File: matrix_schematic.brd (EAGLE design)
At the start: 84.8 x 82.5 mm, 24 parts, among them IC1 74LS595D, IC2 74LS595D, IC3 74LS595D, Q1 MOSFET-NCHANNELBS270, Q2 MOSFET-NCHANNELBS270, Q3 MOSFET-NCHANNELBS270, Q4 MOSFET-NCHANNELBS270

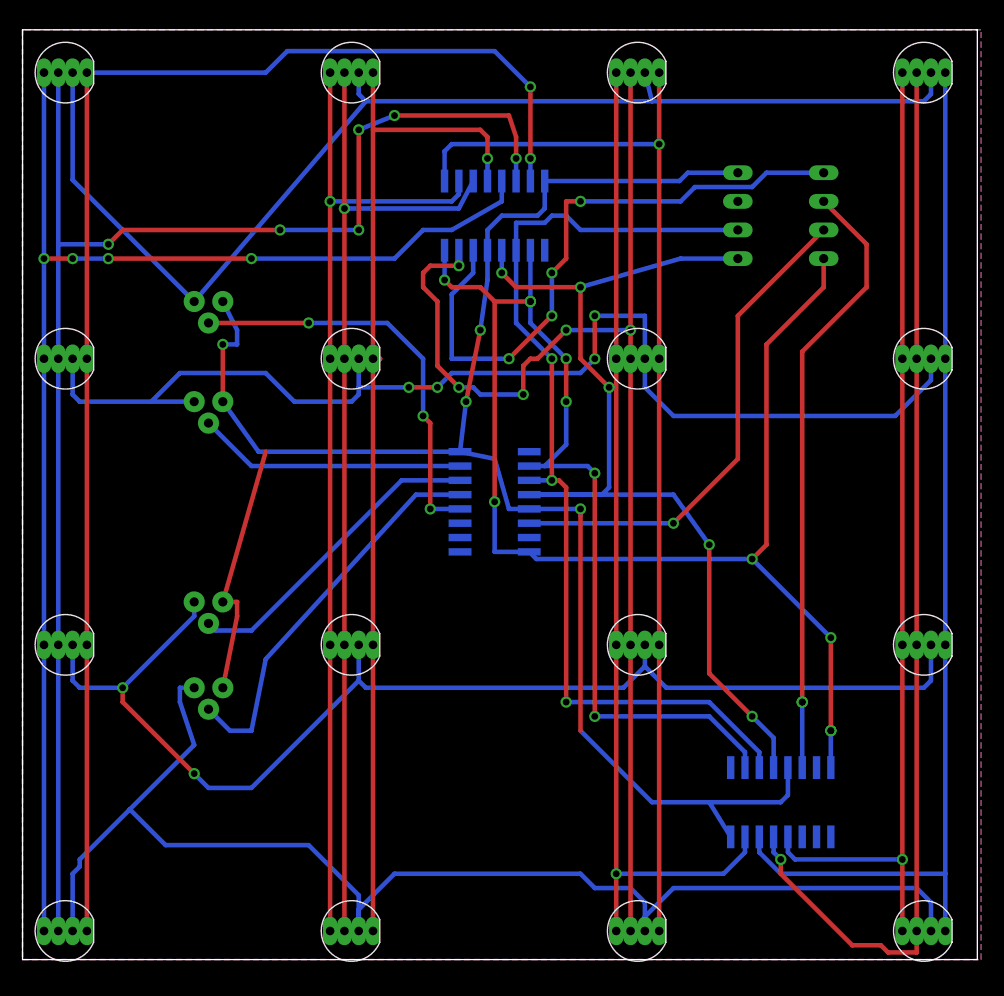
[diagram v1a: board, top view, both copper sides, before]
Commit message: Fixed a bunch of overlaps
Still many overlaps, the RGB LED footprint I used overlaps every pad.
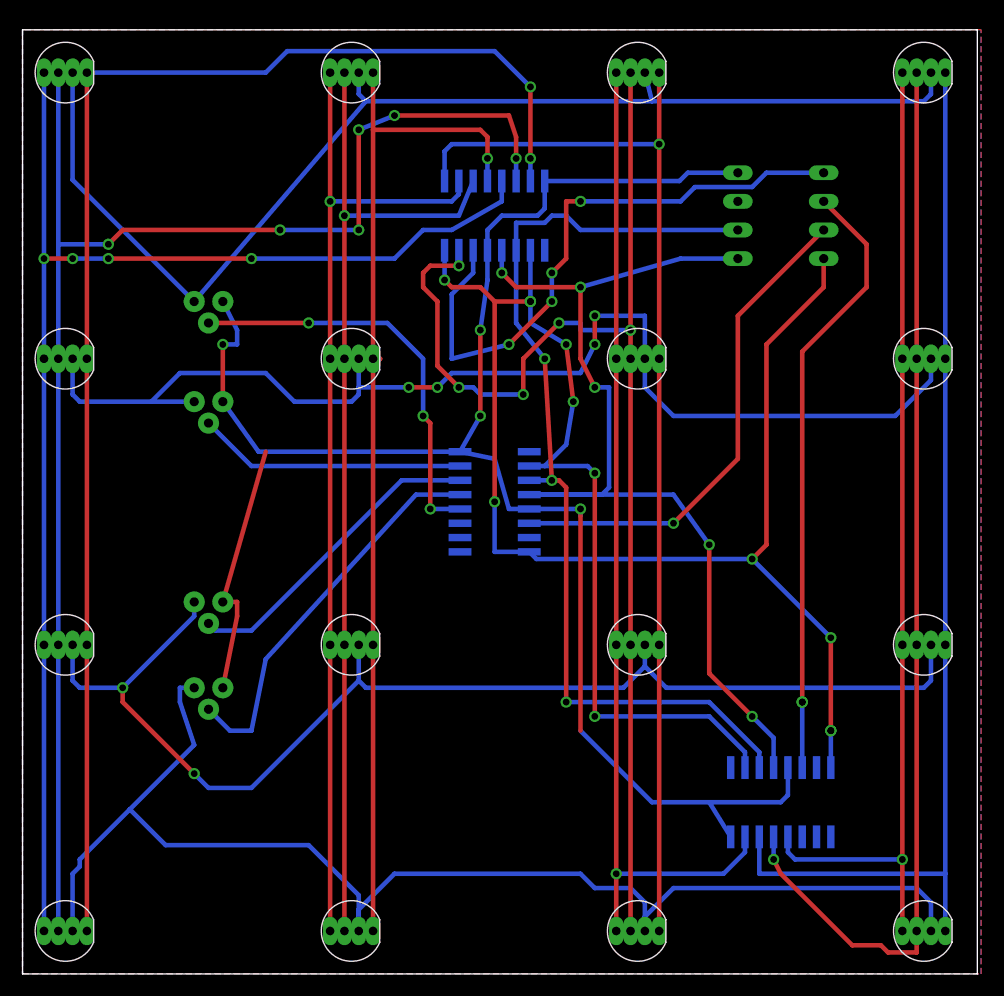
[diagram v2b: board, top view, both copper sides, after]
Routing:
- net N$9: track 111.8 -> 113.1 mm
- net N$7: track 94.9 -> 96.0 mm
- net N$23: track 55.5 -> 54.4 mm
- net N$24: track 89.1 -> 89.7 mm
- net VCC: track 172.1 -> 172.6 mm
- net N$2: track 90.4 -> 91.0 mm
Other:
- board size 84.8 x 82.5 mm -> 84.8 x 83.8 mm
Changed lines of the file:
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@@
 <board>
 <plain>
-<wire x1="0" y1="0" x2="84.76" y2="0" width="0" layer="20"/>
-<wire x1="84.76" y1="0" x2="84.76" y2="82.54" width="0" layer="20"/>
+<wire x1="0" y1="-1.27" x2="84.76" y2="-1.27" width="0" layer="20"/>
+<wire x1="84.76" y1="-1.27" x2="84.76" y2="82.54" width="0" layer="20"/>
 <wire x1="84.76" y1="82.54" x2="0" y2="82.54" width="0" layer="20"/>
-<wire x1="0" y1="82.54" x2="0" y2="0" width="0" layer="20"/>
+<wire x1="0" y1="82.54" x2="0" y2="-1.27" width="0" layer="20"/>
 </plain>
 <attributes>
@@
 <contactref element="Q2" pad="3"/>
 <polygon width="0.4064" layer="16">
-<vertex x="0" y="0"/>
-<vertex x="85.09" y="0"/>
+<vertex x="0" y="-1.27"/>
+<vertex x="85.09" y="-1.27"/>
 <vertex x="85.09" y="82.55"/>
 <vertex x="0" y="82.55"/>
 </polygon>
 <polygon width="0.4064" layer="1">
-<vertex x="0" y="0"/>
-<vertex x="85.09" y="0"/>
+<vertex x="0" y="-1.27"/>
+<vertex x="85.09" y="-1.27"/>
 <vertex x="85.09" y="82.55"/>
 <vertex x="0" y="82.55"/>
@@
 <wire x1="19.05" y1="54.61" x2="19.05" y2="55.88" width="0.4064" layer="16"/>
 <wire x1="19.05" y1="55.88" x2="17.78" y2="58.42" width="0.4064" layer="16"/>
-<wire x1="38.8366" y1="45.085" x2="39.37" y2="49.53" width="0.4064" layer="16"/>
-<via x="39.37" y="49.53" extent="1-16" drill="0.6" shape="square"/>
-<wire x1="39.37" y1="49.53" x2="40.64" y2="55.88" width="0.4064" layer="1"/>
+<wire x1="38.8366" y1="45.085" x2="40.64" y2="48.26" width="0.4064" layer="16"/>
+<via x="40.64" y="48.26" extent="1-16" drill="0.6" shape="square"/>
+<wire x1="40.64" y1="48.26" x2="40.64" y2="55.88" width="0.4064" layer="1"/>
 <via x="40.64" y="55.88" extent="1-16" drill="0.6" shape="square"/>
 <wire x1="40.64" y1="55.88" x2="41.275" y2="60.325" width="0.4064" layer="16"/>
@@
 <wire x1="45.085" y1="62.9666" x2="45.085" y2="58.42" width="0.4064" layer="16"/>
 <wire x1="45.085" y1="58.42" x2="45.085" y2="56.515" width="0.4064" layer="16"/>
-<wire x1="45.085" y1="56.515" x2="48.26" y2="53.34" width="0.4064" layer="16"/>
+<wire x1="45.085" y1="56.515" x2="48.26" y2="54.61" width="0.4064" layer="16"/>
 <wire x1="44.9834" y1="43.815" x2="46.355" y2="43.815" width="0.4064" layer="16"/>
 <wire x1="46.355" y1="43.815" x2="48.26" y2="45.72" width="0.4064" layer="16"/>
-<wire x1="48.26" y1="45.72" x2="48.26" y2="49.53" width="0.4064" layer="16"/>
-<via x="48.26" y="49.53" extent="1-16" drill="0.6" shape="square"/>
-<via x="48.26" y="53.34" extent="1-16" drill="0.6" shape="square"/>
-<wire x1="48.26" y1="49.53" x2="48.26" y2="53.34" width="0.4064" layer="1"/>
+<wire x1="48.26" y1="45.72" x2="48.895" y2="49.53" width="0.4064" layer="16"/>
+<via x="48.895" y="49.53" extent="1-16" drill="0.6" shape="square"/>
+<via x="48.26" y="54.61" extent="1-16" drill="0.6" shape="square"/>
+<wire x1="48.895" y1="49.53" x2="48.26" y2="54.61" width="0.4064" layer="1"/>
 <wire x1="46.355" y1="43.815" x2="50.165" y2="43.815" width="0.4064" layer="16"/>
 <wire x1="50.165" y1="43.815" x2="50.8" y2="43.18" width="0.4064" layer="16"/>
@@
 <wire x1="51.435" y1="41.275" x2="52.07" y2="41.91" width="0.4064" layer="16"/>
 <wire x1="52.07" y1="41.91" x2="52.07" y2="50.8" width="0.4064" layer="16"/>
-<via x="52.07" y="50.8" extent="1-16" drill="0.6" shape="square"/>
-<wire x1="52.07" y1="50.8" x2="49.53" y2="53.34" width="0.4064" layer="1"/>
+<wire x1="52.07" y1="50.8" x2="50.8" y2="50.8" width="0.4064" layer="16"/>
+<via x="50.8" y="50.8" extent="1-16" drill="0.6" shape="square"/>
+<wire x1="50.8" y1="50.8" x2="49.53" y2="53.34" width="0.4064" layer="1"/>
 <wire x1="49.53" y1="53.34" x2="49.53" y2="59.69" width="0.4064" layer="1"/>
 <contactref element="ATTINY85" pad="1"/>
@@
 <via x="48.26" y="22.86" extent="1-16" drill="0.6" shape="square"/>
 <wire x1="48.26" y1="22.86" x2="48.26" y2="41.91" width="0.4064" layer="1"/>
-<wire x1="43.815" y1="56.515" x2="46.99" y2="53.34" width="0.4064" layer="16"/>
-<via x="46.99" y="53.34" extent="1-16" drill="0.6" shape="square"/>
-<wire x1="46.99" y1="53.34" x2="46.99" y2="42.545" width="0.4064" layer="1"/>
+<wire x1="43.815" y1="56.515" x2="46.355" y2="53.34" width="0.4064" layer="16"/>
+<via x="46.355" y="53.34" extent="1-16" drill="0.6" shape="square"/>
+<wire x1="46.355" y1="53.34" x2="46.99" y2="42.545" width="0.4064" layer="1"/>
 <contactref element="ATTINY85" pad="2"/>
 <wire x1="63.5" y1="64.77" x2="49.53" y2="64.77" width="0.4064" layer="16"/>
@@
 <wire x1="81.915" y1="27.94" x2="81.915" y2="7.62" width="0.4064" layer="16"/>
 <wire x1="81.915" y1="7.62" x2="81.915" y2="2.54" width="0.4064" layer="16"/>
-<wire x1="65.405" y1="10.8966" x2="65.405" y2="9.525" width="0.4064" layer="16"/>
-<wire x1="65.405" y1="9.525" x2="67.31" y2="7.62" width="0.4064" layer="16"/>
-<wire x1="67.31" y1="7.62" x2="81.915" y2="7.62" width="0.4064" layer="16"/>
+<wire x1="65.405" y1="10.8966" x2="65.405" y2="7.62" width="0.4064" layer="16"/>
+<wire x1="65.405" y1="7.62" x2="81.915" y2="7.62" width="0.4064" layer="16"/>
 </signal>
 <signal name="N$8">
@@
 <wire x1="36.83" y1="50.8" x2="38.1" y2="52.07" width="0.4064" layer="16"/>
 <wire x1="38.1" y1="52.07" x2="49.53" y2="52.07" width="0.4064" layer="16"/>
-<wire x1="49.53" y1="52.07" x2="50.8" y2="53.34" width="0.4064" layer="16"/>
-<via x="50.8" y="53.34" extent="1-16" drill="0.6" shape="square"/>
-<wire x1="50.8" y1="53.34" x2="50.8" y2="57.15" width="0.4064" layer="1"/>
+<wire x1="49.53" y1="52.07" x2="50.8" y2="54.61" width="0.4064" layer="16"/>
+<via x="50.8" y="54.61" extent="1-16" drill="0.6" shape="square"/>
+<wire x1="50.8" y1="54.61" x2="50.8" y2="57.15" width="0.4064" layer="1"/>
 <via x="50.8" y="57.15" extent="1-16" drill="0.6" shape="square"/>
 <wire x1="50.8" y1="57.15" x2="55.245" y2="57.15" width="0.4064" layer="16"/>
@@
 <wire x1="48.26" y1="62.23" x2="46.99" y2="60.96" width="0.4064" layer="1"/>
 <via x="46.99" y="60.96" extent="1-16" drill="0.6" shape="square"/>
-<wire x1="46.99" y1="60.96" x2="46.99" y2="57.15" width="0.4064" layer="16"/>
-<via x="46.99" y="57.15" extent="1-16" drill="0.6" shape="square"/>
-<wire x1="46.99" y1="57.15" x2="43.18" y2="53.34" width="0.4064" layer="1"/>
-<via x="43.18" y="53.34" extent="1-16" drill="0.6" shape="square"/>
-<wire x1="43.18" y1="53.34" x2="38.1" y2="53.34" width="0.4064" layer="16"/>
+<wire x1="46.99" y1="60.96" x2="46.99" y2="58.42" width="0.4064" layer="16"/>
+<via x="46.99" y="58.42" extent="1-16" drill="0.6" shape="square"/>
+<wire x1="46.99" y1="58.42" x2="43.18" y2="54.61" width="0.4064" layer="1"/>
+<via x="43.18" y="54.61" extent="1-16" drill="0.6" shape="square"/>
+<wire x1="43.18" y1="54.61" x2="38.1" y2="53.34" width="0.4064" layer="16"/>
 <wire x1="38.1" y1="53.34" x2="38.1" y2="59.055" width="0.4064" layer="16"/>
 <wire x1="38.1" y1="59.055" x2="40.005" y2="60.96" width="0.4064" layer="16"/>
@@
 <contactref element="D3" pad="3"/>
 <contactref element="IC3" pad="3"/>
-<wire x1="28.575" y1="78.74" x2="28.575" y2="66.675" width="0.4064" layer="1"/>
-<wire x1="28.575" y1="66.675" x2="28.575" y2="53.34" width="0.4064" layer="1"/>
+<wire x1="28.575" y1="78.74" x2="28.575" y2="66.04" width="0.4064" layer="1"/>
+<wire x1="28.575" y1="66.04" x2="28.575" y2="53.34" width="0.4064" layer="1"/>
 <wire x1="28.575" y1="53.34" x2="28.575" y2="27.94" width="0.4064" layer="1"/>
 <wire x1="28.575" y1="27.94" x2="28.575" y2="2.54" width="0.4064" layer="1"/>
-<wire x1="40.005" y1="69.1134" x2="38.735" y2="66.675" width="0.4064" layer="16"/>
-<wire x1="38.735" y1="66.675" x2="28.575" y2="66.675" width="0.4064" layer="16"/>
-<via x="28.575" y="66.675" extent="1-16" drill="0.6" shape="square"/>
+<wire x1="40.005" y1="69.1134" x2="38.735" y2="66.04" width="0.4064" layer="16"/>
+<wire x1="38.735" y1="66.04" x2="28.575" y2="66.04" width="0.4064" layer="16"/>
+<via x="28.575" y="66.04" extent="1-16" drill="0.6" shape="square"/>
 </signal>
 <signal name="N$9">
@@
 <wire x1="40.64" y1="50.165" x2="44.45" y2="50.165" width="0.4064" layer="16"/>
 <via x="44.45" y="50.165" extent="1-16" drill="0.6" shape="square"/>
-<wire x1="44.45" y1="50.165" x2="44.45" y2="52.705" width="0.4064" layer="1"/>
-<wire x1="44.45" y1="52.705" x2="45.085" y2="53.34" width="0.4064" layer="1"/>
-<wire x1="45.085" y1="53.34" x2="45.72" y2="53.34" width="0.4064" layer="1"/>
-<wire x1="45.72" y1="53.34" x2="48.26" y2="55.88" width="0.4064" layer="1"/>
-<via x="48.26" y="55.88" extent="1-16" drill="0.6" shape="square"/>
-<wire x1="48.26" y1="55.88" x2="53.975" y2="55.88" width="0.4064" layer="16"/>
+<wire x1="44.45" y1="50.165" x2="44.45" y2="53.34" width="0.4064" layer="1"/>
+<wire x1="44.45" y1="53.34" x2="47.625" y2="56.515" width="0.4064" layer="1"/>
+<via x="47.625" y="56.515" extent="1-16" drill="0.6" shape="square"/>
+<wire x1="47.625" y1="56.515" x2="49.53" y2="56.515" width="0.4064" layer="16"/>
+<wire x1="49.53" y1="56.515" x2="49.53" y2="55.88" width="0.4064" layer="16"/>
+<wire x1="49.53" y1="55.88" x2="53.975" y2="55.88" width="0.4064" layer="16"/>
 <via x="53.975" y="55.88" extent="1-16" drill="0.6" shape="square"/>
 </signal>
@@
 <wire x1="79.375" y1="27.94" x2="79.375" y2="2.54" width="0.4064" layer="1"/>
 <contactref element="IC2" pad="5"/>
-<wire x1="66.675" y1="10.8966" x2="66.675" y2="9.525" width="0.4064" layer="16"/>
-<wire x1="66.675" y1="9.525" x2="67.31" y2="8.89" width="0.4064" layer="16"/>
-<via x="67.31" y="8.89" extent="1-16" drill="0.6" shape="square"/>
-<wire x1="67.31" y1="8.89" x2="67.31" y2="7.62" width="0.4064" layer="1"/>
+<wire x1="66.675" y1="10.8966" x2="66.675" y2="8.89" width="0.4064" layer="16"/>
+<via x="66.675" y="8.89" extent="1-16" drill="0.6" shape="square"/>
+<wire x1="66.675" y1="8.89" x2="67.31" y2="7.62" width="0.4064" layer="1"/>
 <wire x1="67.31" y1="7.62" x2="73.66" y2="1.27" width="0.4064" layer="1"/>
 <wire x1="73.66" y1="1.27" x2="76.2" y2="1.27" width="0.4064" layer="1"/>

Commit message: Added ISP header for programming
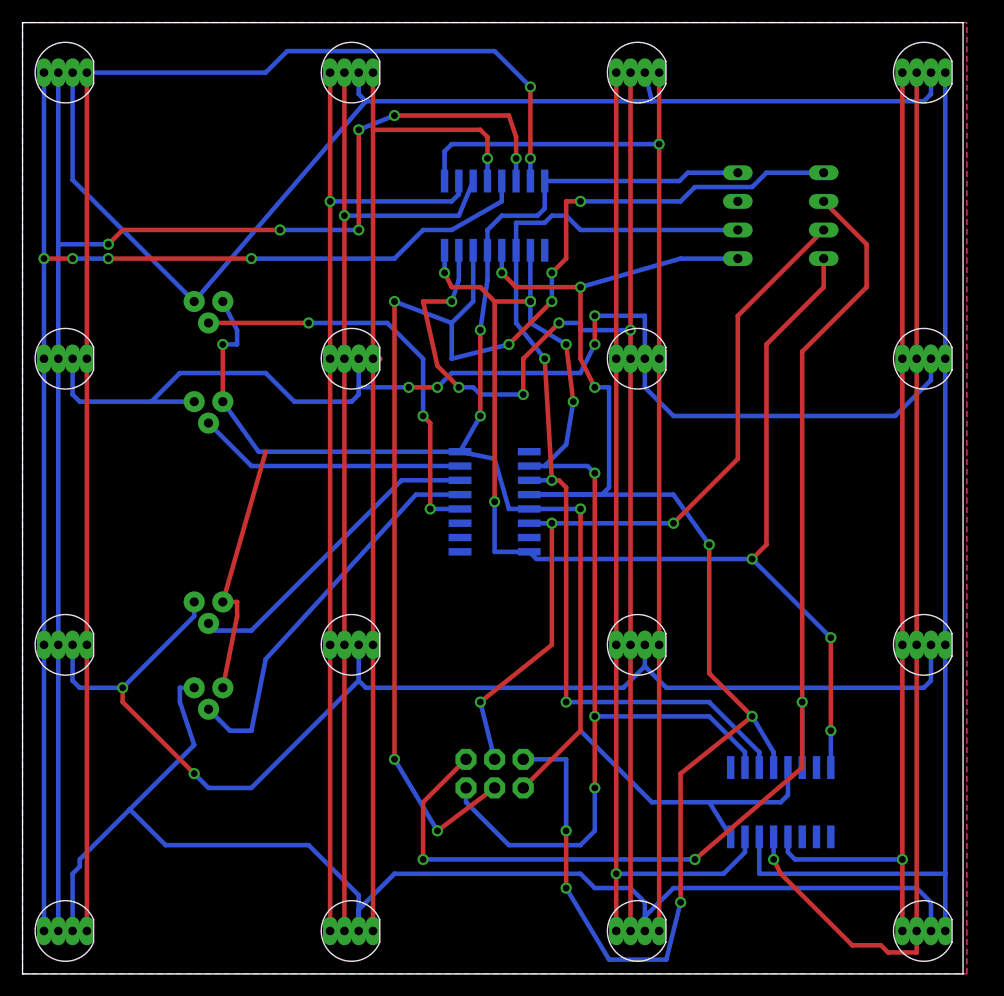
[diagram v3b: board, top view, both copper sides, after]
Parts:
- added J1: AVR_SPI_PRG_6PTH, SparkFun-Connectors:2X3
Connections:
- net GND: now also J1.6
- net N$2: now also J1.5
- net N$21: now also J1.3
- net N$22: now also J1.1
- net N$23: now also J1.4
- net VCC: now also J1.2
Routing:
- net N$23: track 54.4 -> 114.2 mm, vias 4 -> 7
- net N$22: track 54.2 -> 107.2 mm, vias 1 -> 3
- net N$2: track 91.0 -> 143.2 mm, vias 5 -> 8
- net VCC: track 172.6 -> 197.5 mm, vias 11 -> 12
- net N$21: track 44.4 -> 68.5 mm, vias 1 -> 3
- net GND: track 164.4 -> 171.6 mm
- net N$9: track 113.1 -> 112.6 mm
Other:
- board size 84.8 x 83.8 mm -> 83.5 x 84.4 mm
